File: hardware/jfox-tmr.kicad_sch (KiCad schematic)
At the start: 0 parts

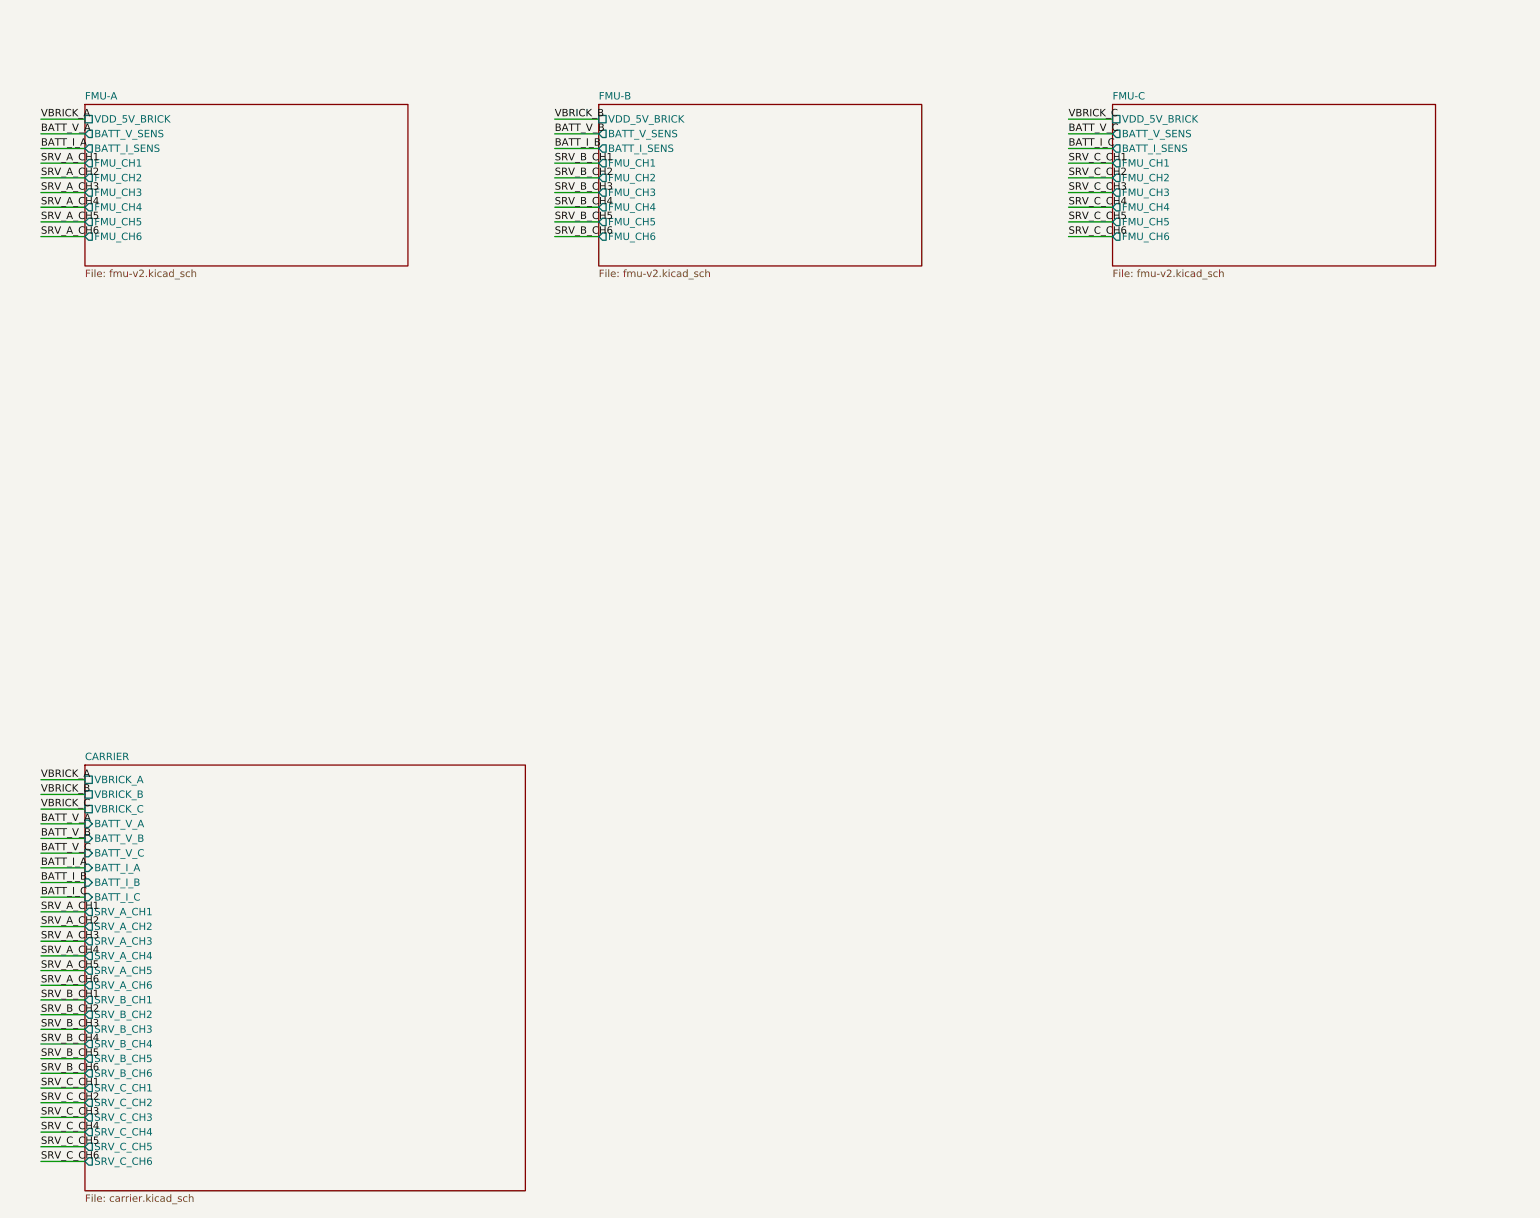
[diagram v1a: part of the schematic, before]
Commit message: Take the carrier from schematic to a DRC-clean board; fix a dangling-net defect
Exporting the carrier as a standalone board netlist exposed a real design
defect: 28 of its nets terminated on a single pin. As a child sheet of
jfox-tmr that reads fine - the net continues into the FMU sheet - but a
pass-through carrier is a path, and half a path is not one. Each board had a
single power connector with nowhere for the power to go.

Redesigned so every signal enters on one connector and leaves on another:
brick power in (J4-J6) -> module J601 out (J7-J9), CAN to the modules
(J1-J3) daisy-chained. Nine connectors, twelve nets, zero single-pin nets.

Two things are deliberately no longer on this board. The servo/PWM breakout
is gone because how three boards' motor commands arbitrate into one output
is still unresolved - TmrVoter is not wired into motor_task - and copper is
the wrong place to record a guess; each module's J901 cables straight to its
ESCs meanwhile. The safety switch is gone because J702's SAFETY lands on
U801.PB5, the IO co-processor this firmware never runs, and neither J405 nor
J601 carries a pin to route it through, so it would have been decorative.

The carrier is now its own KiCad project. It has to be: the three FMU
modules are separately manufactured hardware, and a shared project would
make a board netlist try to place 421 module components on the carrier.

Board work:

- All nine connectors carry real footprints - Hirose DF13 vertical parts
  matching what the modules actually use.
- tools/gen_carrier_pcb.py writes an 80x60 mm two-layer outline with four M3
  holes on a 30.000 x 30.000 mm pattern. That pattern is read from the
  module's own PX4FMUv2.4.5.brd via `kicad-cli pcb import` - board import
  exists on the CLI even though schematic import does not - so a stacked
  module lines up rather than nearly lining up.
- Verified: DRC 0 violations, 0 unconnected. Gerbers, drill and job file all
  export; the drill file contains exactly four 3.2 mm N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
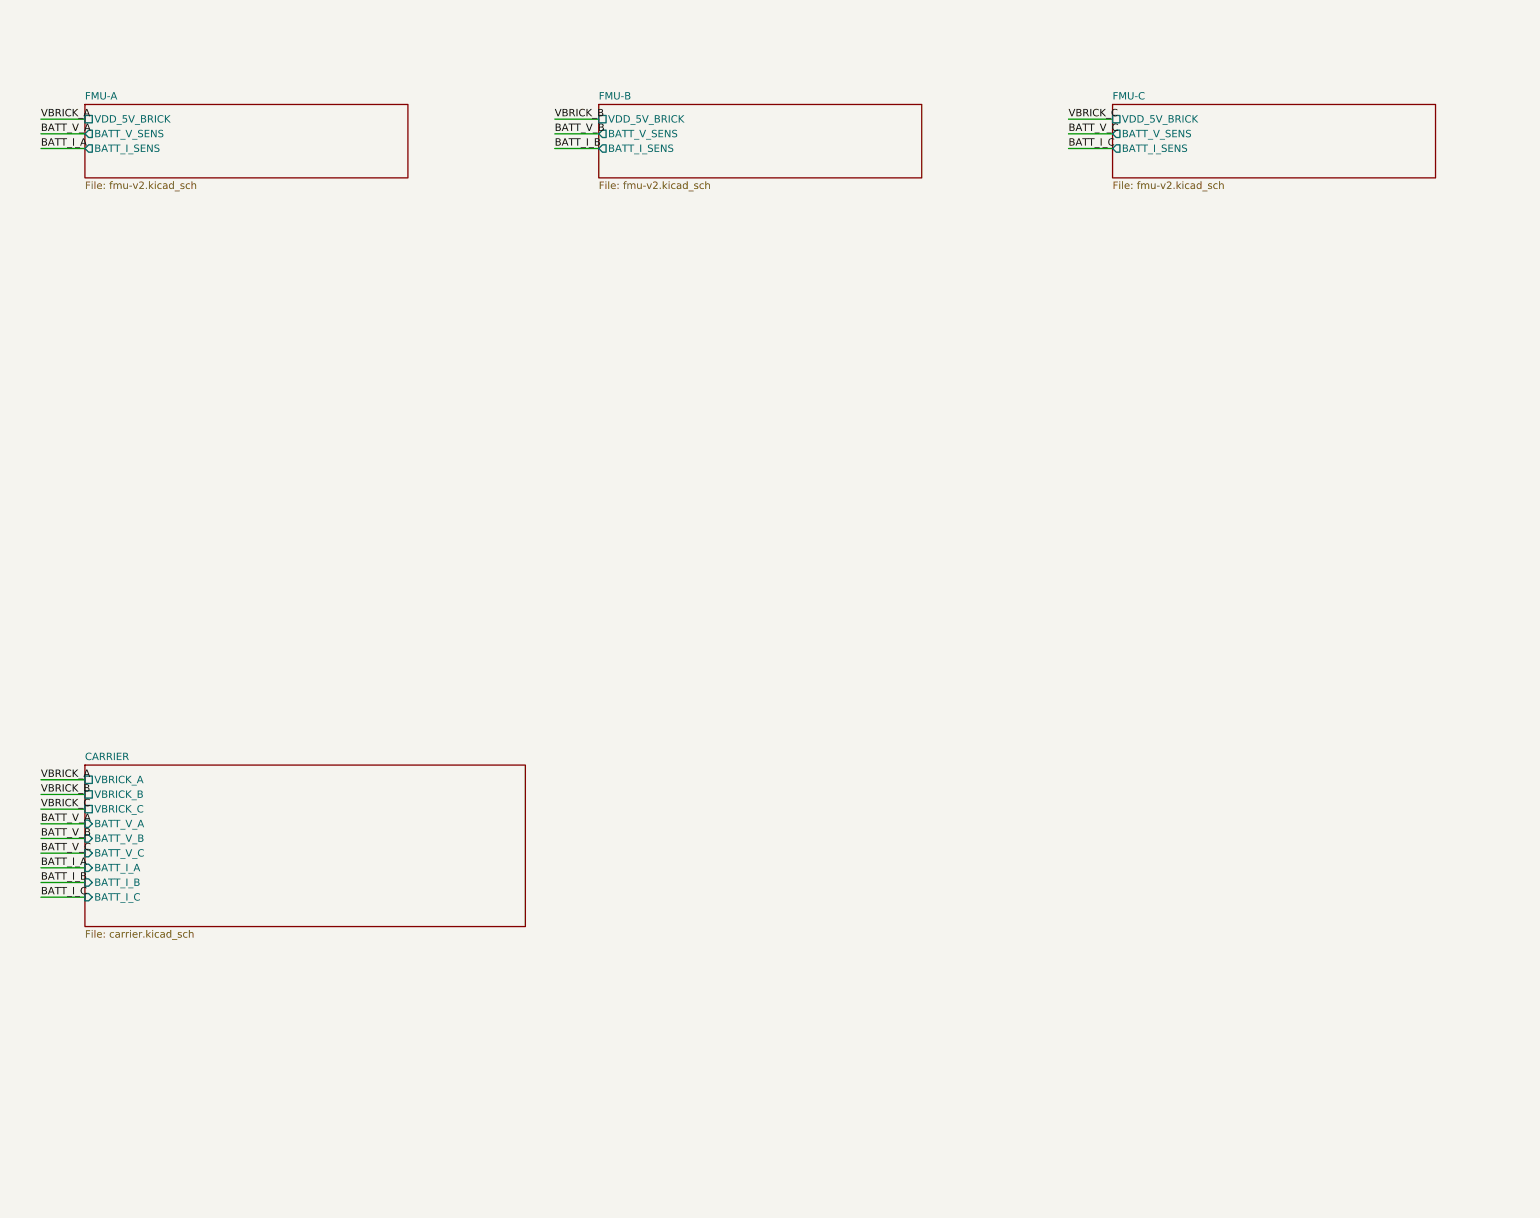
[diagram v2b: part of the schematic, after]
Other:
- sheet CARRIER ports: added none; removed SRV_A_CH1, SRV_A_CH2, SRV_A_CH3, SRV_A_CH4, SRV_A_CH5, SRV_A_CH6, SRV_B_CH1, SRV_B_CH2, SRV_B_CH3, SRV_B_CH4, SRV_B_CH5, SRV_B_CH6, SRV_C_CH1, SRV_C_CH2, SRV_C_CH3, SRV_C_CH4, SRV_C_CH5, SRV_C_CH6
- sheet FMU-A ports: added none; removed FMU_CH1, FMU_CH2, FMU_CH3, FMU_CH4, FMU_CH5, FMU_CH6
- sheet FMU-B ports: added none; removed FMU_CH1, FMU_CH2, FMU_CH3, FMU_CH4, FMU_CH5, FMU_CH6
- sheet FMU-C ports: added none; removed FMU_CH1, FMU_CH2, FMU_CH3, FMU_CH4, FMU_CH5, FMU_CH6

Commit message: Complete the 3-board TMR system: real board instances, verified independent
The three FMU sheets were placeholders. They are now three instances of the
real 492-symbol board, and the array's defining property - three boards that
fail independently but share one voting bus - is demonstrable from KiCad's
netlist rather than asserted.

The blocker was that KiCad's Eagle import wires every cross-page net as a
global label: 136 distinct, 123 spanning pages, no internal hierarchy.
Global means global to the whole project, so instantiating that design three
times would have shorted all 120 non-shared nets together across FMU-A/B/C -
every SPI bus, every MCU pin, every internal rail - while looking completely
normal on screen.

gen_fmu_hierarchical.py generates hardware/fmu-v2/ from the pristine import,
which stays untouched and re-importable: 120 multi-page nets become
hierarchical labels plus sheet pins on a new container root, joined there by
local labels, so connectivity survives but is scoped to one instance; 12
single-page nets become local labels; CAN_H/CAN_L/GND/SAFETY stay global,
which is correct, since those four are what the modules genuinely share.

That is heavy automated surgery on a design nobody can eyeball, so
check_fmu_conversion.py exports a netlist from the pristine import and from
the converted copy and compares them net by net: 262 multi-pin nets on both
sides, joining exactly the same pins.

annotate_tmr_instances.py then gives each instance its own designators
(C101 -> C101A/B/C) by writing one (path ...) entry per instance, the
mechanism KiCad's own test project uses for a thrice-instantiated subsheet.
It derives the hierarchy prefix from the files rather than assuming it -
KiCad 10 roots symbol paths at the root document's uuid, KiCad 7 did not, and
the imported pages use a third form. Assuming any one of them silently gave
all three boards the "A" reference.

Verified on the full system netlist:
  885 component instances, 885 distinct references,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
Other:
- sheet FMU-A: file fmu-v2.kicad_sch -> fmu-v2/fmu-v2.kicad_sch
- sheet FMU-A ports: added BATT_CURRENT_SENS, BATT_VOLTAGE_SENS; removed BATT_I_SENS, BATT_V_SENS
- sheet FMU-B: file fmu-v2.kicad_sch -> fmu-v2/fmu-v2.kicad_sch
- sheet FMU-B ports: added BATT_CURRENT_SENS, BATT_VOLTAGE_SENS; removed BATT_I_SENS, BATT_V_SENS
- sheet FMU-C: file fmu-v2.kicad_sch -> fmu-v2/fmu-v2.kicad_sch
- sheet FMU-C ports: added BATT_CURRENT_SENS, BATT_VOLTAGE_SENS; removed BATT_I_SENS, BATT_V_SENS
- note added: "JFOX-FCU - 3-board TMR system.\nFMU-A/B/C are three instances of ONE sheet (fmu-v2/). Editing it\nedits all three; KiCad keeps their reference designators distinct via the\nper-instance paths. CAN_H/CAN_L/GND/SAFETY are global labels because all\nthree boards genuinely share those nets. Power and servo signals are\nhierarchical pins so each board's stay separate - which is the entire point."
- note removed: "JFOX-FCU - 3-board TMR system.\nFMU-A/B/C are three instances of ONE sheet (fmu-v2.kicad_sch). Editing it\nedits all three; KiCad keeps their reference designators distinct via the\nper-instance paths. CAN_H/CAN_L/GND/SAFETY are global labels because all\nthree boards genuinely share those nets. Power and servo signals are\nhierarchical pins so each board's stay separate - which is the entire poi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"
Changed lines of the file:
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@@
 (kicad_sch (version 20230819) (generator eeschema)
   (paper "A3")
-  (text "JFOX-FCU - 3-board TMR system.\\nFMU-A/B/C are three instances of ONE sheet (fmu-v2.kicad_sch). Editing it\\nedits all three; KiCad keeps their reference designators distinct via the\\nper-instance paths. CAN_H/CAN_L/GND/SAFETY are global labels because all\\nthree boards genuinely share those nets. Power and servo signals are\\nhierarchical pins so each board's stay separate - which is the entire point." (at 25.4 20.32 0)
+  (text "JFOX-FCU - 3-board TMR system.\\nFMU-A/B/C are three instances of ONE sheet (fmu-v2/). Editing it\\nedits all three; KiCad keeps their reference designators distinct via the\\nper-instance paths. CAN_H/CAN_L/GND/SAFETY are global labels because all\\nthree boards genuinely share those nets. Power and servo signals are\\nhierarchical pins so each board's stay separate - which is the entire point." (at 25.4 20.32 0)
     (effects (font (size 1.27 1.27)) (justify left top))
   )
@@
       (effects (font (size 1.27 1.27)) (justify left bottom))
     )
-    (property "Sheetfile" "fmu-v2.kicad_sch" (at 38.1 89.4846 0)
+    (property "Sheetfile" "fmu-v2/fmu-v2.kicad_sch" (at 38.1 89.4846 0)
       (effects (font (size 1.27 1.27)) (justify left top))
     )
@@
       (effects (font (size 1.27 1.27)) (justify right))
     )
-    (pin "BATT_V_SENS" output (at 38.1 81.28 180)
+    (pin "BATT_CURRENT_SENS" output (at 38.1 81.28 180)
       (effects (font (size 1.27 1.27)) (justify right))
     )
-    (pin "BATT_I_SENS" output (at 38.1 83.82 180)
+    (pin "BATT_VOLTAGE_SENS" output (at 38.1 83.82 180)
       (effects (font (size 1.27 1.27)) (justify right))
     )
     (instances
       (project "jfox-tmr"
-        (path "/b3ef39c1-da53-43cd-b9ee-5acf701187a5" (page "2"))
+        (path "/0aa4df91-bba1-44a5-8b0f-5997e6fd590b" (page "2"))
       )
     )
@@
     (stroke (width 0) (type default))
   )
-  (label "BATT_V_A" (at 30.48 81.28000000000002 180)
+  (label "BATT_I_A" (at 30.48 81.28000000000002 180)
     (effects (font (size 1.27 1.27)) (justify left bottom))
   )
@@
     (stroke (width 0) (type default))
   )
-  (label "BATT_I_A" (at 30.48 83.82000000000002 180)
+  (label "BATT_V_A" (at 30.48 83.82000000000002 180)
     (effects (font (size 1.27 1.27)) (justify left bottom))
   )
@@
       (effects (font (size 1.27 1.27)) (justify left bottom))
     )
-    (property "Sheetfile" "fmu-v2.kicad_sch" (at 127.0 89.4846 0)
+    (property "Sheetfile" "fmu-v2/fmu-v2.kicad_sch" (at 127.0 89.4846 0)
       (effects (font (size 1.27 1.27)) (justify left top))
     )
@@
       (effects (font (size 1.27 1.27)) (justify right))
     )
-    (pin "BATT_V_SENS" output (at 127.0 81.28 180)
+    (pin "BATT_CURRENT_SENS" output (at 127.0 81.28 180)
       (effects (font (size 1.27 1.27)) (justify right))
     )
-    (pin "BATT_I_SENS" output (at 127.0 83.82 180)
+    (pin "BATT_VOLTAGE_SENS" output (at 127.0 83.82 180)
       (effects (font (size 1.27 1.27)) (justify right))
     )
     (instances
       (project "jfox-tmr"
-        (path "/b3ef39c1-da53-43cd-b9ee-5acf701187a5" (page "3"))
+        (path "/0aa4df91-bba1-44a5-8b0f-5997e6fd590b" (page "3"))
       )
     )
@@
     (stroke (width 0) (type default))
   )
-  (label "BATT_V_B" (at 119.38 81.28000000000002 180)
+  (label "BATT_I_B" (at 119.38 81.28000000000002 180)
     (effects (font (size 1.27 1.27)) (justify left bottom))
   )
@@
     (stroke (width 0) (type default))
   )
-  (label "BATT_I_B" (at 119.38 83.82000000000002 180)
+  (label "BATT_V_B" (at 119.38 83.82000000000002 180)
     (effects (font (size 1.27 1.27)) (justify left bottom))
   )
@@
       (effects (font (size 1.27 1.27)) (justify left bottom))
     )
-    (property "Sheetfile" "fmu-v2.kicad_sch" (at 215.9 89.4846 0)
+    (property "Sheetfile" "fmu-v2/fmu-v2.kicad_sch" (at 215.9 89.4846 0)
       (effects (font (size 1.27 1.27)) (justify left top))
     )
@@
       (effects (font (size 1.27 1.27)) (justify right))
     )
-    (pin "BATT_V_SENS" output (at 215.9 81.28 180)
+    (pin "BATT_CURRENT_SENS" output (at 215.9 81.28 180)
       (effects (font (size 1.27 1.27)) (justify right))
     )
-    (pin "BATT_I_SENS" output (at 215.9 83.82 180)
+    (pin "BATT_VOLTAGE_SENS" output (at 215.9 83.82 180)
       (effects (font (size 1.27 1.27)) (justify right))
     )
     (instances
       (project "jfox-tmr"
-        (path "/b3ef39c1-da53-43cd-b9ee-5acf701187a5" (page "4"))
+        (path "/0aa4df91-bba1-44a5-8b0f-5997e6fd590b" (page "4"))
       )
     )
@@
     (stroke (width 0) (type default))
   )
-  (label "BATT_V_C" (at 208.28 81.28000000000002 180)
+  (label "BATT_I_C" (at 208.28 81.28000000000002 180)
     (effects (font (size 1.27 1.27)) (justify left bottom))
   )
@@
     (stroke (width 0) (type default))
   )
-  (label "BATT_I_C" (at 208.28 83.82000000000002 180)
+  (label "BATT_V_C" (at 208.28 83.82000000000002 180)
     (effects (font (size 1.27 1.27)) (justify left bottom))
   )
@@
     (instances
       (project "jfox-tmr"
-        (path "/b3ef39c1-da53-43cd-b9ee-5acf701187a5" (page "5"))
+        (path "/0aa4df91-bba1-44a5-8b0f-5997e6fd590b" (page "5"))
       )
     )

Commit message: Stop the TMR project churning files on open; make annotation idempotent
Three things surfaced from opening the project in KiCad.

"Switch to PCB Editor" on jfox-tmr reports the board file does not exist and
offers to create one. That is correct - jfox-tmr is the system schematic and
has no PCB on purpose, because the three FMU modules are separately
manufactured hardware rather than parts to place; a board made from it would
try to lay out ~885 components. Saying yes would produce exactly the wrong
thing, so the warning is now on the schematic's own root sheet and in
hardware/README.md, which also tabulates the two projects and which one is
the board.

Merely opening the project showed sixteen modified files. The generator emits
KiCad 7 syntax - that being the version there are real reference files for -
and KiCad rewrites them to its own format on first open. gen_tmr_schematic.py
now runs `kicad-cli sch upgrade` on its output, so what is committed is
already in the installed KiCad's format and opening changes nothing.

annotate_tmr_instances.py was not idempotent. It read the existing reference
out of each instances block and appended a board letter, so a second run
turned C1102A into C1102AA and a third into C1102CAA. It now strips any
trailing board letters before appending; references are stable across
repeated runs, verified by running it three times.

Also fixes gen_fmu_hierarchical.py failing to clear its output directory:
KiCad's Local History feature leaves a git repo there, git marks its objects
read-only, and rmtree dies with EACCES on Windows.

Verified after: connectivity still identical to the pristine import, the
carrier is still DRC clean with 0 unconnected, and host tests pass.

Co-Authored-By: Claude Opus 5 <noreply@anthropic.com>
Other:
- note added: "THIS PROJECT HAS NO PCB, ON PURPOSE.\n'Switch to PCB Editor' will offer to create one - say no. The three FMU\nmodules are separately manufactured boards, not parts to be placed; a board\nmade from this schematic would try to lay out ~885 components.\nThe PCB is the carrier alone: open hardware/carrier/carrier.kicad_pro."
